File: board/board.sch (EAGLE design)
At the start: 1 part

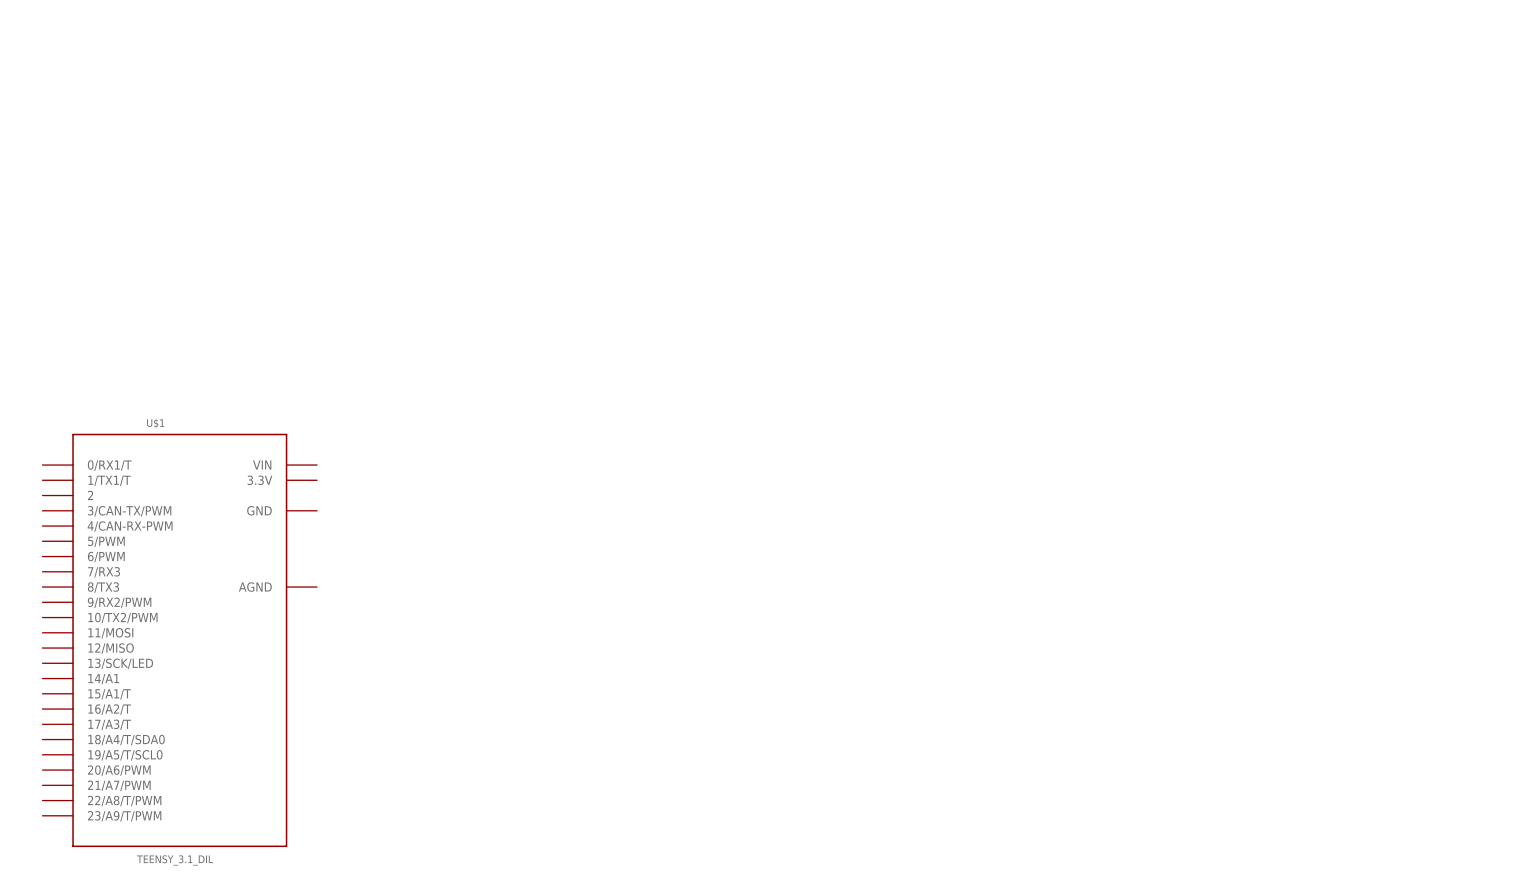
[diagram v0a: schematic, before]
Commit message: Add and arrange components for controlling piezo
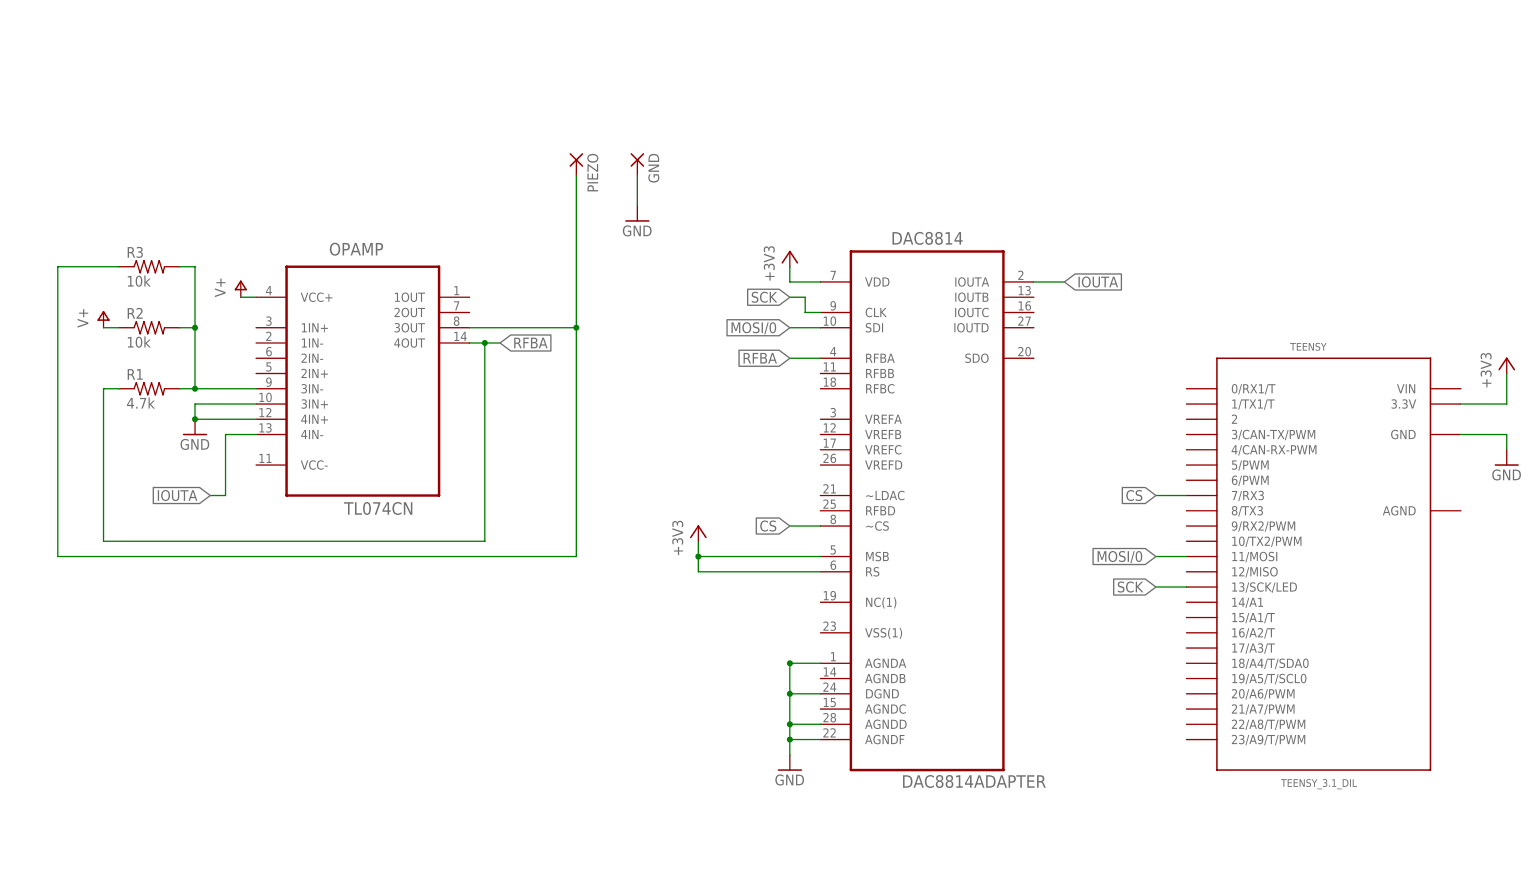
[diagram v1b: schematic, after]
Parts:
- removed U$1: TEENSY_3.1_DIL, Teensy_3_and_LC_Series_Boards_v1.1:TEENSY_3.1_DIL
- added DAC8814: DAC8814ADAPTER, board:DAC8814ADAPTER
- added GND, PIEZO: (no value), wirepad:1,6/0,8
- added OPAMP: TL074CN, Texas Instruments_By_element14_Batch_1:TL074CN
- added R1: 4.7k, resistor:R-US_0204/7
- added R2, R3: 10k, resistor:R-US_0204/5
- added TEENSY: TEENSY_3.1_DIL, Teensy_3_and_LC_Series_Boards_v1.1:TEENSY_3.1_DIL
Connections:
- new net +3V3: DAC8814.MSB, DAC8814.RS, DAC8814.VDD, TEENSY.3.3V
- new net CS: DAC8814.~CS, TEENSY.7/RX3
- new net GND: DAC8814.AGNDA, DAC8814.AGNDD, DAC8814.AGNDF, DAC8814.DGND, GND.P, OPAMP.3IN+, OPAMP.4IN+, TEENSY.GND
- new net IOUTA: DAC8814.IOUTA, OPAMP.4IN-
- new net MOSI/0: DAC8814.SDI, TEENSY.11/MOSI
- new net N$1: OPAMP.3IN-, R1.2, R2.2, R3.2
- new net N$5: OPAMP.3OUT, PIEZO.P, R3.1
- new net RFBA: DAC8814.RFBA, OPAMP.4OUT, R1.1
- new net SCK: DAC8814.CLK, TEENSY.13/SCK/LED
- new net V+: OPAMP.VCC+, R2.1

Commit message: Add missing connections
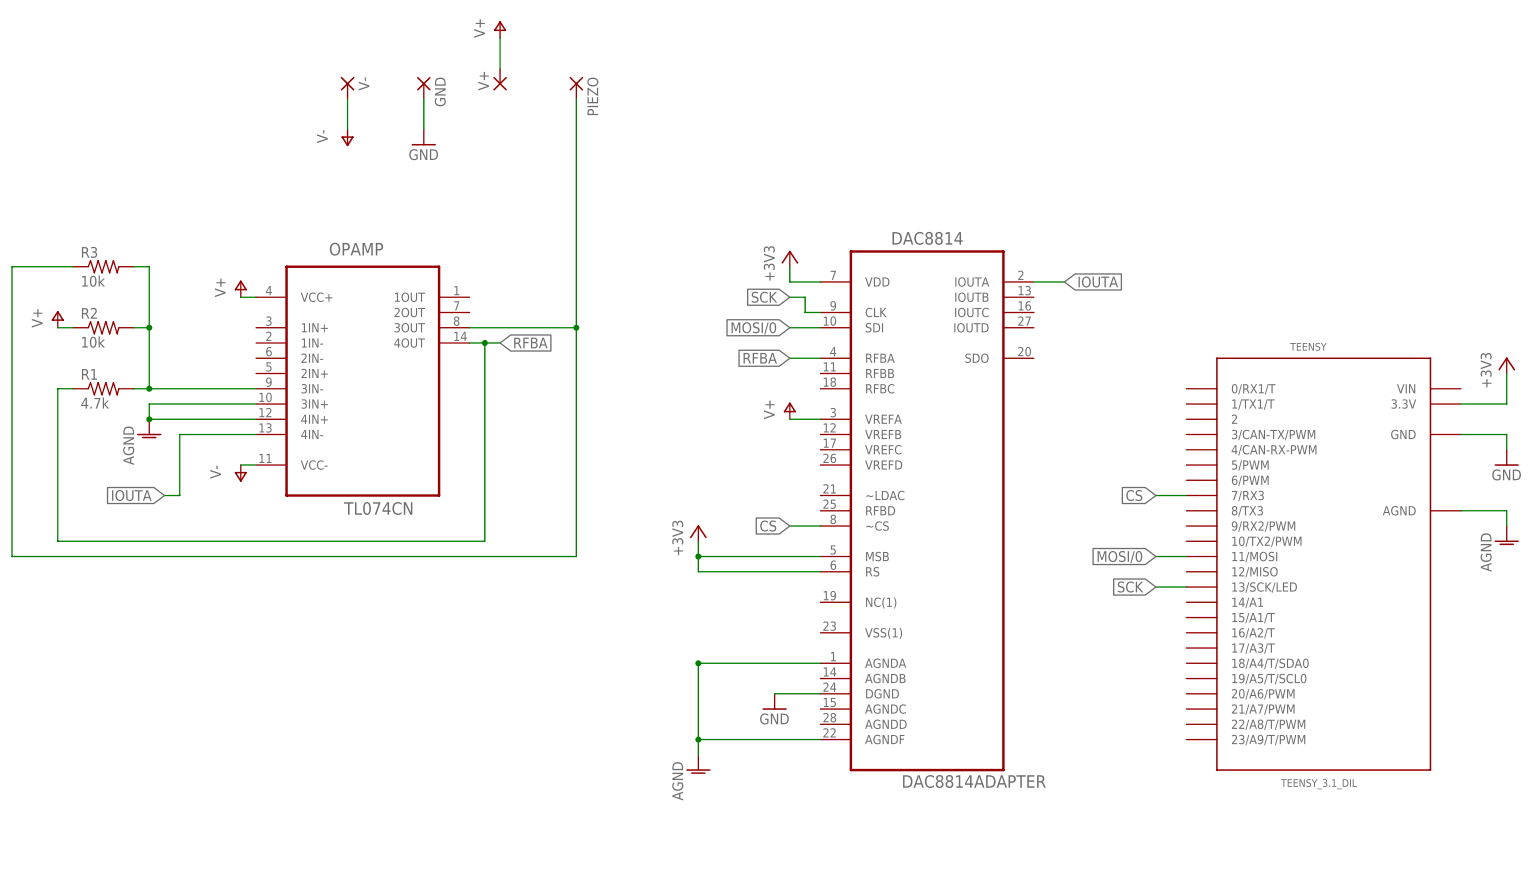
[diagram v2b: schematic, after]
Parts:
- added V+, V-: (no value), wirepad:1,6/0,8
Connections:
- new net AGND: DAC8814.AGNDA, DAC8814.AGNDF, OPAMP.3IN+, OPAMP.4IN+, TEENSY.AGND
- new net V-: OPAMP.VCC-, V-.P
- net GND: no longer DAC8814.AGNDA, DAC8814.AGNDD, DAC8814.AGNDF, OPAMP.3IN+, OPAMP.4IN+
- net V+: now also DAC8814.VREFA, V+.P
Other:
- moved on the sheet: GND, PIEZO, R1, R2, R3
